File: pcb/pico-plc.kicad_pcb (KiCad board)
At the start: 2 copper layers, 154.5 x 95.5 mm, 172 parts, among them J1 Conn_02x06_Odd_Even, J12 Screw_Terminal_01x02, J13 Screw_Terminal_01x02, J15 Conn_01x03, J16 Conn_01x03, J18 Screw_Terminal_01x03, J19 Screw_Terminal_01x03, J2 Conn_01x06, J20 Screw_Terminal_01x03, J21 Screw_Terminal_01x03, J22 Screw_Terminal_01x03, J23 Screw_Terminal_01x03, J24 Screw_Terminal_01x03, J25 Screw_Terminal_01x03, J26 Screw_Terminal_01x02, J27 Screw_Terminal_01x02, J28 Screw_Terminal_01x02, J29 Screw_Terminal_01x02, J3 Conn_02x06_Odd_Even, J30 Screw_Terminal_01x02, J31 Screw_Terminal_01x02, J32 Screw_Terminal_01x02, J33 Screw_Terminal_01x02, J5 Conn_01x06, J6 Conn_01x06, J7 Screw_Terminal_01x02, J8 Conn_01x02, K1 Relay_SPDT, K2 Relay_SPDT, K3 Relay_SPDT, K4 Relay_SPDT, K5 Relay_SPDT, K6 Relay_SPDT, K7 Relay_SPDT, K8 Relay_SPDT, Q1 BSS138, Q10 NDS355AN, Q11 NDS355AN, Q12 NDS355AN, Q13 NDS355AN, Q14 NDS355AN, Q15 NDS355AN, Q2 BSS138, Q3 BSS138, Q4 BSS138, Q5 BSS138, Q6 BSS138, Q7 BSS138, Q8 NDS355AN, Q9 NDS355AN, U1 DS18B20, U2 VO615A, U3 VO615A, U4 VO615A, U5 VO615A, U6 VO615A, U7 VO615A, U8 VO615A, U9 VO615A

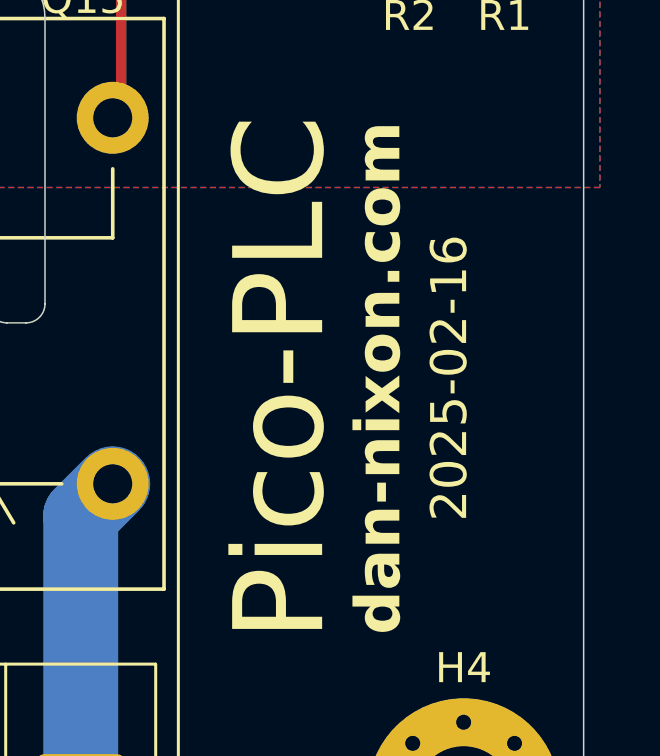
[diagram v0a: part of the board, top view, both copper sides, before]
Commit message: pcb: disconnect mounting holes from GND, fix dimension annotations
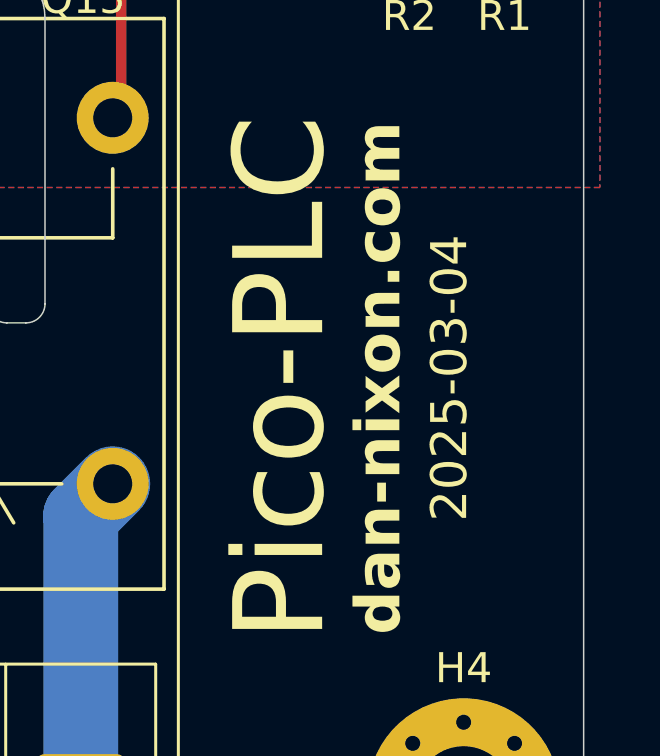
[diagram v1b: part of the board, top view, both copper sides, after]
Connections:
- H1 pad 1: GND -> unconnected-(H1-Pad1)_8
- H2 pad 1: GND -> unconnected-(H2-Pad1)_7
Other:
- board text added: "2025-03-04"
- board text removed: "2025-02-16"
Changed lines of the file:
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@@
 	(net 164 "unconnected-(H4-Pad1)_7")
 	(net 165 "unconnected-(H4-Pad1)_8")
+	(net 166 "unconnected-(H1-Pad1)")
+	(net 167 "unconnected-(H1-Pad1)_1")
+	(net 168 "unconnected-(H1-Pad1)_2")
+	(net 169 "unconnected-(H1-Pad1)_3")
+	(net 170 "unconnected-(H1-Pad1)_4")
+	(net 171 "unconnected-(H1-Pad1)_5")
+	(net 172 "unconnected-(H1-Pad1)_6")
+	(net 173 "unconnected-(H1-Pad1)_7")
+	(net 174 "unconnected-(H1-Pad1)_8")
+	(net 175 "unconnected-(H2-Pad1)")
+	(net 176 "unconnected-(H2-Pad1)_1")
+	(net 177 "unconnected-(H2-Pad1)_2")
+	(net 178 "unconnected-(H2-Pad1)_3")
+	(net 179 "unconnected-(H2-Pad1)_4")
+	(net 180 "unconnected-(H2-Pad1)_5")
+	(net 181 "unconnected-(H2-Pad1)_6")
+	(net 182 "unconnected-(H2-Pad1)_7")
+	(net 183 "unconnected-(H2-Pad1)_8")
 	(footprint "Diode_SMD:D_SOD-123"
 		(layer "F.Cu")
@@
 			(layers "*.Cu" "*.Mask")
 			(remove_unused_layers no)
-			(net 3 "GND")
+			(net 167 "unconnected-(H1-Pad1)_1")
 			(pinfunction "1")
-			(pintype "input")
+			(pintype "input+no_connect")
 			(zone_connect 2)
 		)
@@
 			(layers "*.Cu" "*.Mask")
 			(remove_unused_layers no)
-			(net 3 "GND")
+			(net 171 "unconnected-(H1-Pad1)_5")
 			(pinfunction "1")
-			(pintype "input")
+			(pintype "input+no_connect")
 			(zone_connect 2)
 		)
@@
 			(layers "*.Cu" "*.Mask")
 			(remove_unused_layers no)
-			(net 3 "GND")
+			(net 170 "unconnected-(H1-Pad1)_4")
 			(pinfunction "1")
-			(pintype "input")
+			(pintype "input+no_connect")
 			(zone_connect 2)
 		)
@@
 			(layers "*.Cu" "*.Mask")
 			(remove_unused_layers no)
-			(net 3 "GND")
+			(net 172 "unconnected-(H1-Pad1)_6")
 			(pinfunction "1")
-			(pintype "input")
+			(pintype "input+no_connect")
 			(zone_connect 2)
 		)
@@
 			(layers "*.Cu" "*.Mask")
 			(remove_unused_layers no)
-			(net 3 "GND")
+			(net 173 "unconnected-(H1-Pad1)_7")
 			(pinfunction "1")
-			(pintype "input")
+			(pintype "input+no_connect")
 		)
 		(pad "1" thru_hole circle
@@
 			(layers "*.Cu" "*.Mask")
 			(remove_unused_layers no)
-			(net 3 "GND")
+			(net 166 "unconnected-(H1-Pad1)")
 			(pinfunction "1")
-			(pintype "input")
+			(pintype "input+no_connect")
 			(zone_connect 2)
 		)
@@
 			(layers "*.Cu" "*.Mask")
 			(remove_unused_layers no)
-			(net 3 "GND")
+			(net 168 "unconnected-(H1-Pad1)_2")
 			(pinfunction "1")
-			(pintype "input")
+			(pintype "input+no_connect")
 			(zone_connect 2)
 		)
@@
 			(layers "*.Cu" "*.Mask")
 			(remove_unused_layers no)
-			(net 3 "GND")
+			(net 169 "unconnected-(H1-Pad1)_3")
 			(pinfunction "1")
-			(pintype "input")
+			(pintype "input+no_connect")
 			(zone_connect 2)
 		)
@@
 			(layers "*.Cu" "*.Mask")
 			(remove_unused_layers no)
-			(net 3 "GND")
+			(net 174 "unconnected-(H1-Pad1)_8")
 			(pinfunction "1")
-			(pintype "input")
+			(pintype "input+no_connect")
 			(zone_connect 2)
 		)
@@
 			(layers "*.Cu" "*.Mask")
 			(remove_unused_layers no)
-			(net 3 "GND")
+			(net 177 "unconnected-(H2-Pad1)_2")
 			(pinfunction "1")
-			(pintype "input")
+			(pintype "input+no_connect")
 			(zone_connect 2)
 		)
@@
 			(layers "*.Cu" "*.Mask")
 			(remove_unused_layers no)
-			(net 3 "GND")
+			(net 181 "unconnected-(H2-Pad1)_6")
 			(pinfunction "1")
-			(pintype "input")
+			(pintype "input+no_connect")
 			(zone_connect 2)
 		)
@@
 			(layers "*.Cu" "*.Mask")
 			(remove_unused_layers no)
-			(net 3 "GND")
+			(net 183 "unconnected-(H2-Pad1)_8")
 			(pinfunction "1")
-			(pintype "input")
+			(pintype "input+no_connect")
 			(zone_connect 2)
 		)
@@
 			(layers "*.Cu" "*.Mask")
 			(remove_unused_layers no)
-			(net 3 "GND")
+			(net 175 "unconnected-(H2-Pad1)")
 			(pinfunction "1")
-			(pintype "input")
+			(pintype "input+no_connect")
 			(zone_connect 2)
 		)
@@
 			(layers "*.Cu" "*.Mask")
 			(remove_unused_layers no)
-			(net 3 "GND")
+			(net 179 "unconnected-(H2-Pad1)_4")
 			(pinfunction "1")
-			(pintype "input")
+			(pintype "input+no_connect")
 		)
 		(pad "1" thru_hole circle
@@
 			(layers "*.Cu" "*.Mask")
 			(remove_unused_layers no)
-			(net 3 "GND")
+			(net 180 "unconnected-(H2-Pad1)_5")
 			(pinfunction "1")
-			(pintype "input")
+			(pintype "input+no_connect")
 			(zone_connect 2)
 		)
@@
 			(layers "*.Cu" "*.Mask")
 			(remove_unused_layers no)
-			(net 3 "GND")
+			(net 178 "unconnected-(H2-Pad1)_3")
 			(pinfunction "1")
-			(pintype "input")
+			(pintype "input+no_connect")
 			(zone_connect 2)
 		)
@@
 			(layers "*.Cu" "*.Mask")
 			(remove_unused_layers no)
-			(net 3 "GND")
+			(net 176 "unconnected-(H2-Pad1)_1")
 			(pinfunction "1")
-			(pintype "input")
+			(pintype "input+no_connect")
 			(zone_connect 2)
 		)
@@
 			(layers "*.Cu" "*.Mask")
 			(remove_unused_layers no)
-			(net 3 "GND")
+			(net 182 "unconnected-(H2-Pad1)_7")
 			(pinfunction "1")
-			(pintype "input")
+			(pintype "input+no_connect")
 			(zone_connect 2)
 		)
@@
 		)
 	)
-	(gr_text "2025-02-16"
+	(gr_text "2025-03-04"
 		(at 187.325 111.125 90)
 		(layer "F.SilkS")
@@
 		(layer "User.4")
 		(pts
-			(xy 54 46) (xy 188.5 46)
+			(xy 43 38) (xy 43 133.5)
 		)
-		(height -11.075)
+		(height 11.249999)
 		(format
 			(prefix "")
@@
 			(keep_text_aligned yes)
 		)
-		(gr_text "134.5000 mm"
-			(at 121.25 33.775 0)
+		(gr_text "95.5000 mm"
+			(at 30.600001 85.75 90)
 			(layer "User.4")
 			(effects
@@
 	)
 	(dimension
-		(type aligned)
+		(type orthogonal)
 		(layer "User.4")
 		(pts
-			(xy 43 38) (xy 43 133.5)
+			(xy 192.5 43) (xy 38 43)
 		)
-		(height 11.249999)
+		(height -11.25)
+		(orientation 0)
 		(format
 			(prefix "")
@@
 			(keep_text_aligned yes)
 		)
-		(gr_text "95.5000 mm"
-			(at 30.600001 85.75 90)
+		(gr_text "154.5000 mm"
+			(at 115.25 30.6 0)
 			(layer "User.4")
 			(effects
@@
 	)
 	(dimension
-		(type aligned)
+		(type orthogonal)
 		(layer "User.4")
 		(pts
-			(xy 50 43) (xy 192.5 43)
+			(xy 188.5 46) (xy 42 46)
 		)
-		(height -11.25)
+		(height -11.075)
+		(orientation 0)
 		(format
 			(prefix "")
@@
 			(keep_text_aligned yes)
 		)
-		(gr_text "142.5000 mm"
-			(at 121.25 30.6 0)
+		(gr_text "146.5000 mm"
+			(at 115.25 33.775 0)
 			(layer "User.4")
 			(effects

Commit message: New board revision
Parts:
- removed J12, J13: Screw_Terminal_01x02, Conn_ScrewTerminals:CTB7000-2
- removed J2, J5, J6: Conn_01x06, Connector_PinHeader_2.54mm:PinHeader_1x06_P2.54mm_Vertical
- removed J3: Conn_02x06_Odd_Even, Connector_PinHeader_2.54mm:PinHeader_2x06_P2.54mm_Vertical
- removed JP1, JP2, JP3, JP4, JP5, JP6: Jumper_2_Open, TestPoint:TestPoint_2Pads_Pitch2.54mm_Drill0.8mm
- removed Q2, Q3, Q4, Q5, Q6, Q7: BSS138, Package_TO_SOT_SMD:SOT-23
- removed R10, R11, R12, R13, R14, R15, R16, R5, R6, R7, R8, R9: 10k, Resistor_SMD:R_0805_2012Metric_Pad1.20x1.40mm_HandSolder
- removed TP1: Run, TestPoint:TestPoint_Pad_D2.0mm
- removed TP2: 3.3V En, TestPoint:TestPoint_Pad_D2.0mm
- A1: footprint RaspberryPi_Pico:RaspberryPi_Pico_Common -> Module:RaspberryPi_Pico_Common_THT
- J1: value Conn_02x06_Odd_Even -> Conn_01x09; footprint Connector_PinHeader_2.54mm:PinHeader_2x06_P2.54mm_Vertical -> Connector_PinHeader_2.54mm:PinHeader_1x09_P2.54mm_Vertical
- U2, U3, U4, U5, U6, U7, U8, U9: footprint Package_DIP:SMDIP-4_W7.62mm -> Package_DIP:SMDIP-4_W9.53mm
- moved J7 163.5 mm to (202.5, 125.0), turned to 0 degrees
- moved J8 155.8 mm to (203.8, 118.5), turned to -90 degrees
- moved D1 148.7 mm to (195.5, 118.5), turned to 0 degrees
- moved J1 59.7 mm to (214.0, 90.3), turned to 0 degrees
- moved U1 47.6 mm to (160.5, 68.4), turned to -90 degrees
- moved R3 38.0 mm to (175.7, 71.0)
- moved Q1 38.0 mm to (171.9, 71.0)
- moved R4 38.0 mm to (168.1, 71.0)
- moved H1 31.5 mm to (214.0, 64.5)
- moved D2 29.5 mm to (215.7, 76.5)
- moved D3 29.5 mm to (212.5, 76.5)
- moved R1 29.5 mm to (215.7, 82.2)
- moved R2 29.5 mm to (212.5, 82.2)
- moved J15 26.9 mm to (149.2, 71.5)
- moved J16 26.9 mm to (153.0, 71.5)
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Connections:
- A1 pad 30: /RUN -> unconnected-(A1-RUN-Pad30)
- A1 pad 31: /IO26 -> unconnected-(A1-GPIO26_ADC0-Pad31)
- A1 pad 32: /IO27 -> unconnected-(A1-GPIO27_ADC1-Pad32)
- A1 pad 33: GNDA -> unconnected-(A1-AGND-Pad33)
- A1 pad 35: /ADC_VREF -> unconnected-(A1-ADC_VREF-Pad35)
- A1 pad 37: /3V3_EN -> unconnected-(A1-3V3_EN-Pad37)
- J1 pad 3: GND -> /IO22
- J1 pad 4: +3V3 -> /IO21
- J1 pad 5: GND -> /IO20
- J1 pad 6: +3V3 -> /IO19
- J1 pad 7: GND -> /IO18
- J1 pad 8: +3V3 -> /IO17
- J1 pad 9: GND -> /IO16
- JP21 pad 1: /IO7 -> /IO8
- JP22 pad 1: /IO6 -> /IO9
- JP23 pad 1: /IO16 -> /IO10
- JP24 pad 1: /IO17 -> /IO11
- JP25 pad 1: /IO18 -> /IO12
- JP26 pad 1: /IO19 -> /IO13
- JP27 pad 1: /IO20 -> /IO14
- JP28 pad 1: /IO21 -> /IO15
- JP41 pad 2: /IO15 -> /IO5
- JP42 pad 2: /IO14 -> /IO6
- JP44 pad 2: /IO13 -> /IO7
- JP45 pad 2: /IO12 -> /IO2
- JP47 pad 2: /IO11 -> /IO3
- JP48 pad 2: /IO10 -> /IO4
- JP50 pad 2: /IO9 -> /IO1
- JP51 pad 2: /IO8 -> /IO0
- Q1 pad 2: /IO22 -> /IO28
- R3 pad 2: /IO22 -> /IO28
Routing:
- net /IO0: track 22.7 -> 146.9 mm
- net /IO1: track 20.1 -> 135.1 mm
- net +5V: track 475.8 -> 371.1 mm, vias 15 -> 9
- net +3V3: track 293.7 -> 207.6 mm, vias 15 -> 1
- net /IO2: track 23.7 -> 101.4 mm
- net /IO3: track 36.3 -> 111.5 mm
- net /IO4: track 49.8 -> 121.6 mm
- net /IO16: track 59.7 -> 7.72 mm
- net /IO6: track 120.5 -> 74.6 mm, vias 1 -> 0
- net /IO7: track 126.6 -> 84.8 mm, vias 1 -> 0
- net /IO17: track 46.1 -> 7.72 mm
- net /IO28: track 5.08 -> 39.1 mm, vias 0 -> 1
- net /General IO/IO0_SHIFTED: track 32.9 -> 0.00 mm, vias 1 -> 0
- net /IO18: track 34.2 -> 7.33 mm
- net /General IO/IO1_SHIFTED: track 25.9 -> 0.00 mm, vias 1 -> 0
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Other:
- board size 154.5 x 95.5 mm -> 181.5 x 72 mm
- board text added: "2026-02-25"
- board text added: "C"
- board text added: "In 8"
- board text added: "M3 mounting holes Hole centres: 172.5 x 63 Board size: 181.5 x 72"
- board text added: "Rly. 1"
- board text added: "Rly. 8"
- board text removed: "0"
- board text removed: "1"
- board text removed: "2"
- board text removed: "2025-03-04"
- board text removed: "26"
- board text removed: "27"
- board text removed: "28"
- board text removed: "3"
- board text removed: "3V"
- board text removed: "3V3_EN"
- board text removed: "4"
- board text removed: "5"
- board text removed: "Aux. Power Out"
- board text removed: "G"
- board text removed: "IO"
- board text removed: "In 0"
- board text removed: "In 2"
- board text removed: "In 3"
- board text removed: "In 4"
- board text removed: "In 5"
- board text removed: "In 6"
- board text removed: "In 7"
- board text removed: "JLCJLCJLCJLC"
- board text removed: "M3 mounting holes"
- board text removed: "RUN"
- board text removed: "Relay 0"
- board text removed: "Relay 1"
- board text removed: "Relay 2"
- board text removed: "Relay 3"
- board text removed: "Relay 4"
- board text removed: "Relay 5"
- board text removed: "Relay 6"
- board text removed: "Relay 7"
- board text removed: "Vr"
